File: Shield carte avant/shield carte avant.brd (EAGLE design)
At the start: 68.6 x 53.3 mm, 22 parts, among them IC1 MCP2562-E_SN, IC2 MCP2515-I_SO, J1 22-05-7078-07, J2 22-05-7028-02, J3 22-05-7038-03, J5 22-05-7028-02, M1 ARDUINO_R3_ICSP

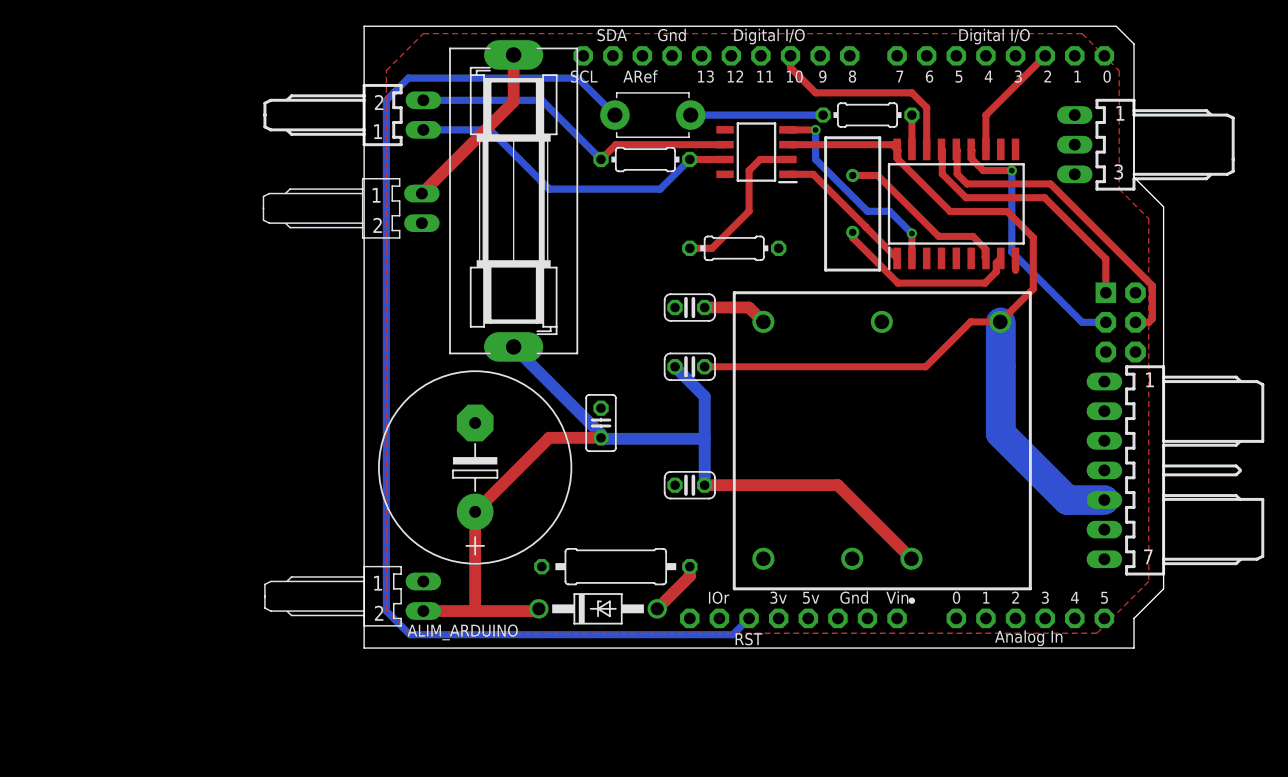
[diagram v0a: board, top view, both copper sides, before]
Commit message: Déplacement de composant pour faire de la place pour les relais
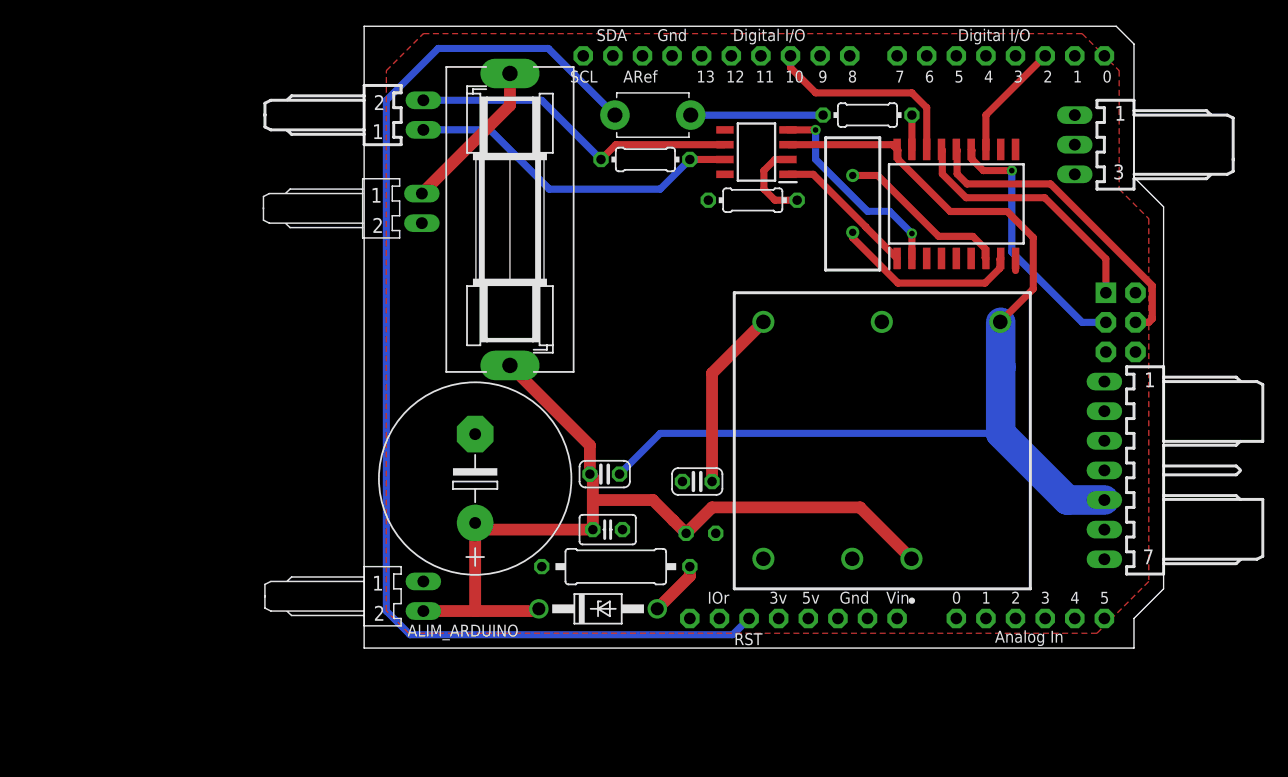
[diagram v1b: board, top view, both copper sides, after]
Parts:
- moved C5 14.9 mm to (29.8, 14.3)
- moved C4 11.8 mm to (21.9, 14.9)
- moved C2 9.16 mm to (22.2, 10.2), turned to 0 degrees
- moved R1 4.42 mm to (34.6, 38.4), turned to 0 degrees
- moved C3 4.24 mm to (30.2, 9.84), flipped to the bottom
- moved F1 1.62 mm to (13.8, 36.8)
- moved C1 0.95 mm to (10.8, 14.5)
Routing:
- net N$3: track 5.55 -> 15.5 mm
- net 12V: track 83.4 -> 76.2 mm
- net +5_V: track 81.0 -> 88.2 mm
- net N$7: track 13.6 -> 7.30 mm
- net RESET: track 98.1 -> 100.2 mm
- net N$1: track 15.1 -> 13.4 mm

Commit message: Alimentation de l'arduino par le 5V, passage des ic CAN en traversant et correction du schéma CAN
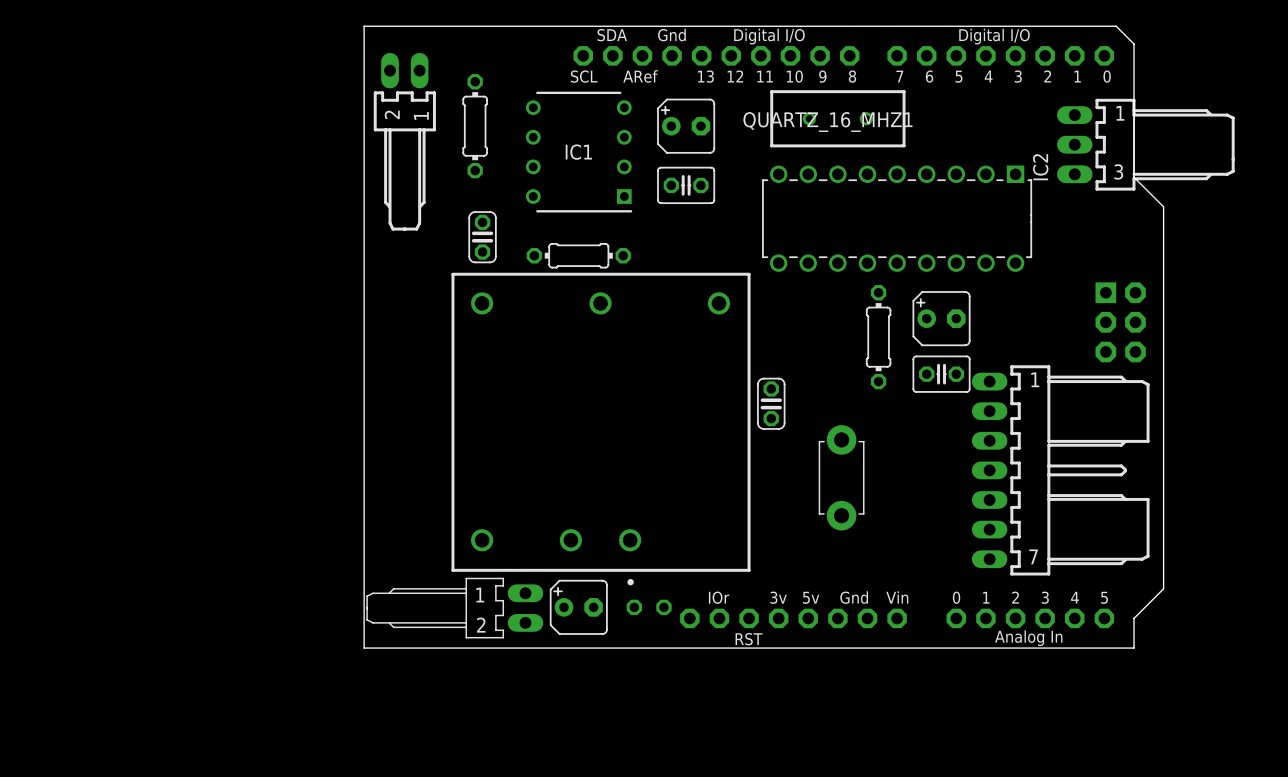
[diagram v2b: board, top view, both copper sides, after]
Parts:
- removed ALIM_ARDUINO: 22-05-7028-02, EP_molex_6410_7395:7395-02
- removed C1: 1mF, rcl:E7,5-16
- removed D1: ZENER 12V, diode:DO41Z10
- removed F1: 4A, fuse:SH25
- removed QUARTZ_16_MHZ: FOXSLF_160-20, FOXSLF_160-20:HC49SLF_1
- removed R20: 0.5, resistor:0309/12
- removed R3: 1k, rcl:0204/7
- removed SW1: (no value), adafruit:TACT_PANA-EVQ
- added C10, C8: 27pF, rcl:C025-030X050
- added C6: (no value), rcl:B45181A
- added C9: 1µF, rcl:B45181A
- added QUARTZ_16_MHZ1: FOXSLF_160-20, FOXSLF_160-20:HC49SLF_1
- added R4: 1k, rcl:0204/7
- added SW2: (no value), adafruit:TACT_PANA-EVQ
- C2: value 22nF -> 1 µF; device rcl:C025-025X050 -> rcl:B45181A
- IC1: value MCP2562-E_SN -> MCP2562-E_P; device MCP2562-E_SN:SOIC127P600X175-8N -> MCP2562-E_P:DIP781W56P254L950H533Q8N
- IC2: value MCP2515-I_SO -> MCP2515-I_P; device MCP2515-I_SO:SOIC127P1030X265-18N -> MCP2515-I_P:DIP254P762X432-18
- R1: value 1k -> 100k
- moved J5 35.4 mm to (15.1, 3.43)
- moved C2 33.9 mm to (50.8, 28.3)
- moved C5 27.9 mm to (11.4, 35.2), turned to 90 degrees
- moved PS1 24.2 mm to (8.89, 32.1)
- moved IC2 16.1 mm to (36.8, 33.0), turned to 270 degrees
- moved R1 15.7 mm to (19.7, 33.7), turned to 180 degrees
- moved C4 15.5 mm to (36.2, 21.0), turned to 270 degrees
- moved IC1 15.2 mm to (19.7, 42.5)
- moved R2 14.9 mm to (10.8, 44.8), turned to 90 degrees
- moved J1 9.84 mm to (54.9, 15.2)
- moved C3 7.75 mm to (25.7, 3.49)
- moved J2 4.13 mm to (4.76, 49.5), turned to 0 degrees
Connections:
- removed net +5_V: C4.1, IC1.3, IC2.18, J1.5, PS1.3
- removed net 12V: ALIM_ARDUINO.2, C1.+, C2.1, C3.1, C4.2, D1.C, F1.2, PS1.1
- removed net N$10: IC2.7, QUARTZ_16_MHZ.2
- removed net N$13: M1.GND@1
- removed net N$14: R3.1, SW1.P$2
- removed net N$15: IC2.17, R3.2
- removed net N$16: M1.GND@3
- removed net N$9: IC1.6, J2.2, R2.1
- removed net RIEN: M1.5V
- new net +12V: C3.1, C4.2, C6.+, J5.1, PS1.1
- new net +5V: C10.1, C2.-, C4.1, C8.2, C9.+, IC1.3, IC2.18, J1.5, M1.5V, PS1.3
- new net N$2: R4.2, SW2.P$1
- new net RX: IC2.2
- new net RXD: IC1.4
- new net TX: IC2.1
- new net TXD: IC1.1
- net GND: now also C10.2, C2.+, C6.-, C8.1, C9.-, IC1.2, M1.GND@1, M1.GND@3; no longer ALIM_ARDUINO.1, C1.-, C2.2, R20.1
- net N$1: now also IC1.8, R1.2; no longer F1.1, J5.1
- net N$11: now also IC2.17, R4.1; no longer IC2.8, QUARTZ_16_MHZ.1
- net N$4: now also IC1.5; no longer D1.A, R20.2
- net N$5: now also IC1.7, J2.2, R2.1; no longer IC1.1, IC2.1
- net N$6: now also IC2.7, QUARTZ_16_MHZ1.2; no longer IC1.4, IC2.2
- net N$7: now also IC2.8, QUARTZ_16_MHZ1.1; no longer IC1.2, R1.2
- net N$8: now also IC1.6; no longer IC1.7
- net RESET: now also SW2.P$2; no longer SW1.P$1
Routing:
- net RESET: track 100.2 -> 0.00 mm
- net +5_V: track 88.2 -> 0.00 mm
- net 12V: track 76.2 -> 0.00 mm
- net N$8: track 29.0 -> 0.00 mm
- net N$9: track 28.5 -> 0.00 mm
- net SI: track 27.3 -> 0.00 mm
- net SCK: track 22.2 -> 0.00 mm, vias 1 -> 0
- net SO: track 22.1 -> 0.00 mm
- net N$6: track 17.9 -> 0.00 mm, vias 2 -> 0
- net CS: track 17.7 -> 0.00 mm
- net N$11: track 16.1 -> 0.00 mm
- net N$3: track 15.5 -> 0.00 mm
- net N$10: track 14.8 -> 0.00 mm
- net N$1: track 13.4 -> 0.00 mm
- net N$5: track 12.4 -> 0.00 mm
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- removed copper zone on layer 1, net GND

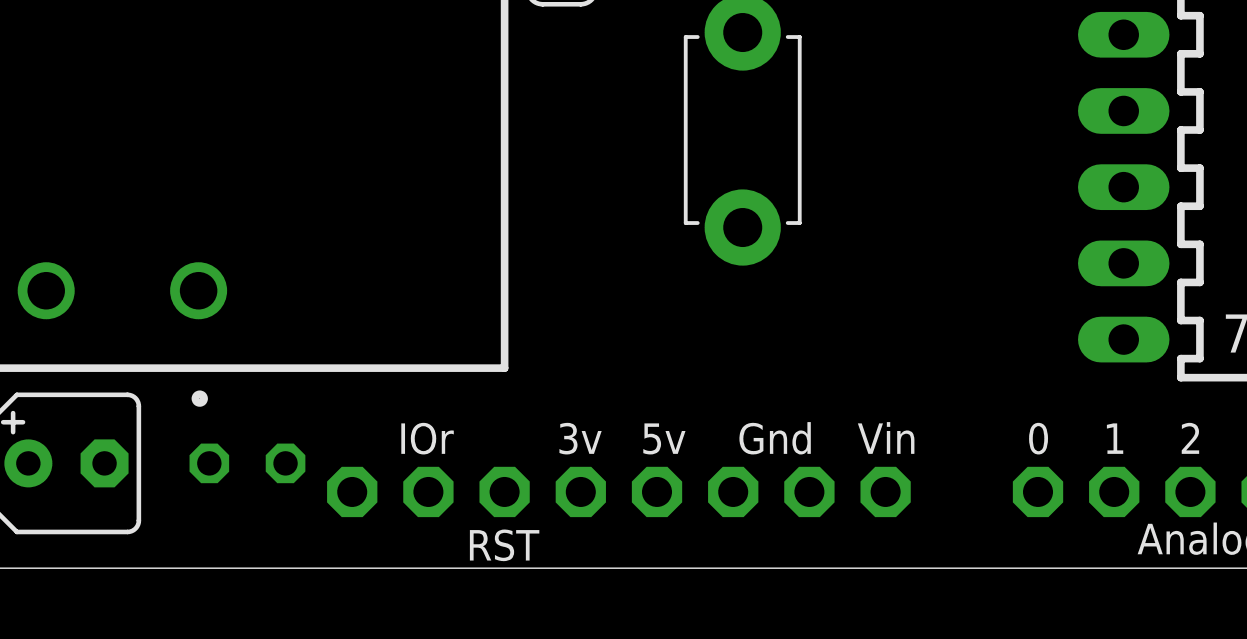
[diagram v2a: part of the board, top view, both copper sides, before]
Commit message: Ajout des résistance de tirage de l'I2C
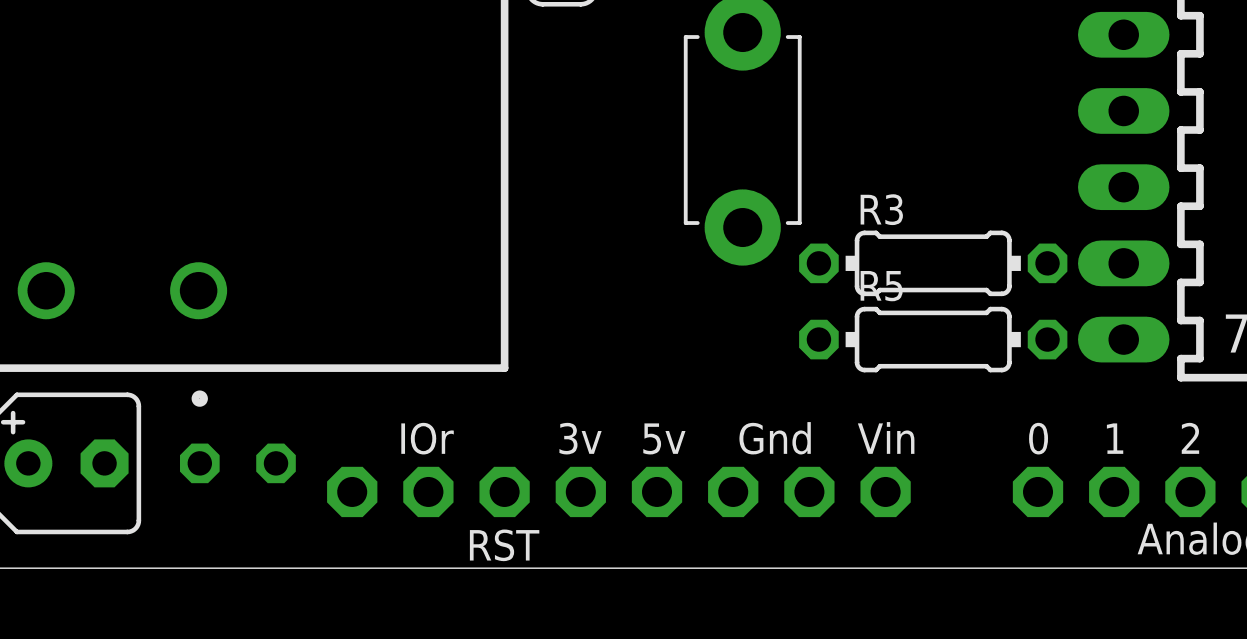
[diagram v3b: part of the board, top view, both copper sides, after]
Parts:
- added R3, R5: 1k, rcl:0204/7
- moved C3 0.32 mm to (25.4, 3.49)
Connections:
- removed net A4: J1.6
- removed net A5: J1.7
- new net SCL: J1.6, M1.A5, R3.2
- new net SDA: J1.7, M1.A4, R5.2
- net +5V: now also R3.1, R5.1
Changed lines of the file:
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@@
 <attribute name="RS_PART_NUMBER" value="0438272P" x="8.89" y="32.0675" size="1.778" layer="27" display="off"/>
 </element>
-<element name="C3" library="rcl" library_urn="urn:adsk.eagle:library:334" package="C025-024X044" package3d_urn="urn:adsk.eagle:package:23630/1" value="4.7 uF" x="25.7175" y="3.4925" smashed="yes" rot="MR180">
-<attribute name="SPICEPREFIX" value="C" x="25.7175" y="3.4925" size="1.778" layer="28" rot="MR180" display="off"/>
-<attribute name="VALUE" x="23.0505" y="5.2705" size="1.27" layer="27" ratio="10"/>
+<element name="C3" library="rcl" library_urn="urn:adsk.eagle:library:334" package="C025-024X044" package3d_urn="urn:adsk.eagle:package:23630/1" value="4.7 uF" x="25.4" y="3.4925" smashed="yes" rot="MR180">
+<attribute name="SPICEPREFIX" value="C" x="25.4" y="3.4925" size="1.778" layer="28" rot="MR180" display="off"/>
+<attribute name="VALUE" x="22.733" y="5.2705" size="1.27" layer="27" ratio="10"/>
 </element>
 <element name="C4" library="rcl" library_urn="urn:adsk.eagle:library:334" package="C025-024X044" package3d_urn="urn:adsk.eagle:package:23630/1" value="680 pF" x="36.195" y="20.955" smashed="yes" rot="R270">
@@
 <attribute name="RS_PART_NUMBER" value="1460216" x="19.685" y="42.545" size="1.778" layer="27" rot="R180" display="off"/>
 <attribute name="VALUE" x="17.4625" y="42.545" size="1.016" layer="27" rot="R270" align="center"/>
+</element>
+<element name="R3" library="rcl" library_urn="urn:adsk.eagle:library:334" package="0204/7" package3d_urn="urn:adsk.eagle:package:23498/1" value="1k" x="48.5775" y="10.16" smashed="yes">
+<attribute name="NAME" x="46.0375" y="11.4554" size="0.9906" layer="25" ratio="10"/>
+<attribute name="SPICEPREFIX" value="R" x="48.5775" y="10.16" size="1.778" layer="27" display="off"/>
+<attribute name="VALUE" x="46.9519" y="9.6774" size="0.9906" layer="27" ratio="10"/>
+</element>
+<element name="R5" library="rcl" library_urn="urn:adsk.eagle:library:334" package="0204/7" package3d_urn="urn:adsk.eagle:package:23498/1" value="1k" x="48.5775" y="7.62" smashed="yes">
+<attribute name="NAME" x="46.0375" y="8.9154" size="0.9906" layer="25" ratio="10"/>
+<attribute name="SPICEPREFIX" value="R" x="48.5775" y="7.62" size="1.778" layer="27" display="off"/>
+<attribute name="VALUE" x="46.9519" y="7.1374" size="0.9906" layer="27" ratio="10"/>
 </element>
 </elements>
@@
 <wire x1="11.43" y1="36.5125" x2="23.495" y2="33.655" width="0" layer="19" extent="1-1"/>
 <wire x1="44.45" y1="2.54" x2="49.53" y2="23.495" width="0" layer="19" extent="1-1"/>
-<wire x1="26.9875" y1="3.4925" x2="44.45" y2="2.54" width="0" layer="19" extent="1-1"/>
-<wire x1="20.955" y1="3.4925" x2="26.9875" y2="3.4925" width="0" layer="19" extent="1-1"/>
+<wire x1="26.67" y1="3.4925" x2="44.45" y2="2.54" width="0" layer="19" extent="1-1"/>
+<wire x1="20.955" y1="3.4925" x2="26.67" y2="3.4925" width="0" layer="19" extent="1-1"/>
 <wire x1="15.113" y1="2.159" x2="20.955" y2="3.4925" width="0" layer="19" extent="1-1"/>
 <wire x1="19.01" y1="9.2475" x2="20.955" y2="3.4925" width="0" layer="19" extent="1-1"/>
@@
 <contactref element="M1" pad="3V"/>
 </signal>
-<signal name="A4">
+<signal name="SDA">
+<contactref element="M1" pad="A4"/>
+<contactref element="R5" pad="2"/>
+<contactref element="J1" pad="7"/>
+<wire x1="54.9275" y1="7.62" x2="62.23" y2="2.54" width="0" layer="19" extent="1-1"/>
+<wire x1="52.3875" y1="7.62" x2="54.9275" y2="7.62" width="0" layer="19" extent="1-1"/>
+</signal>
+<signal name="SCL">
+<contactref element="M1" pad="A5"/>
+<contactref element="R3" pad="2"/>
 <contactref element="J1" pad="6"/>
-</signal>
-<signal name="A5">
-<contactref element="J1" pad="7"/>
+<wire x1="54.9275" y1="10.16" x2="64.77" y2="2.54" width="0" layer="19" extent="1-1"/>
+<wire x1="52.3875" y1="10.16" x2="54.9275" y2="10.16" width="0" layer="19" extent="1-1"/>
 </signal>
 <signal name="D7">
@@
 <contactref element="J5" pad="1"/>
 <wire x1="24.09" y1="9.2475" x2="36.195" y2="19.685" width="0" layer="19" extent="1-1"/>
-<wire x1="24.4475" y1="3.4925" x2="24.09" y2="9.2475" width="0" layer="19" extent="1-1"/>
-<wire x1="18.415" y1="3.4925" x2="24.4475" y2="3.4925" width="0" layer="19" extent="1-1"/>
+<wire x1="24.13" y1="3.4925" x2="24.09" y2="9.2475" width="0" layer="19" extent="1-1"/>
+<wire x1="18.415" y1="3.4925" x2="24.13" y2="3.4925" width="0" layer="19" extent="1-1"/>
 <wire x1="15.113" y1="4.699" x2="18.415" y2="3.4925" width="0" layer="19" extent="1-1"/>
 </signal>
@@
 <contactref element="IC1" pad="3"/>
 <contactref element="J1" pad="5"/>
+<contactref element="R3" pad="1"/>
+<contactref element="R5" pad="1"/>
 <wire x1="52.07" y1="28.2575" x2="57.15" y2="33.02" width="0" layer="19" extent="1-1"/>
 <wire x1="52.07" y1="23.495" x2="52.07" y2="28.2575" width="0" layer="19" extent="1-1"/>
@@
 <wire x1="27.6225" y1="44.7675" x2="27.6225" y2="39.6875" width="0" layer="19" extent="1-1"/>
 <wire x1="23.59" y1="43.815" x2="27.6225" y2="44.7675" width="0" layer="19" extent="1-1"/>
-<wire x1="39.37" y1="2.54" x2="36.195" y2="22.225" width="0" layer="19" extent="1-1"/>
+<wire x1="39.37" y1="2.54" x2="54.9275" y2="12.7" width="0" layer="19" extent="1-1"/>
+<wire x1="44.7675" y1="10.16" x2="39.37" y2="2.54" width="0" layer="19" extent="1-1"/>
+<wire x1="44.7675" y1="7.62" x2="44.7675" y2="10.16" width="0" layer="19" extent="1-1"/>
 </signal>
 <signal name="N$1">

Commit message: Ajout des nouveaux vias
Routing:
- net +5V: track 0.00 -> 99.4 mm
- net +12V: track 0.00 -> 34.9 mm
- net CS: track 0.00 -> 34.8 mm
- net INT: track 0.00 -> 30.9 mm
- net SI: track 0.00 -> 28.2 mm
- net SCK: track 0.00 -> 22.6 mm
- net SCL: track 0.00 -> 17.8 mm
- net SO: track 0.00 -> 17.7 mm
- net N$5: track 0.00 -> 16.7 mm
- net SDA: track 0.00 -> 13.2 mm
- net N$8: track 0.00 -> 12.1 mm
- net RESET: track 0.00 -> 12.1 mm
- net N$11: track 0.00 -> 10.3 mm
- net N$2: track 0.00 -> 6.32 mm
- net N$6: track 0.00 -> 5.77 mm
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- added copper zone on layer 16, net GND
